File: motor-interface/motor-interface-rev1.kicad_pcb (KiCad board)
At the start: 2 copper layers, 43 parts, among them P1 CONN_02X12, P10 CONN_01X03, P11 CONN_01X04, P12 CONN_01X03, P13 CONN_01X03, P2 CONN_02X10, P3 CONN_01X03, P4 CONN_02X10, P5 CONN_01X04, P6 CONN_01X04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

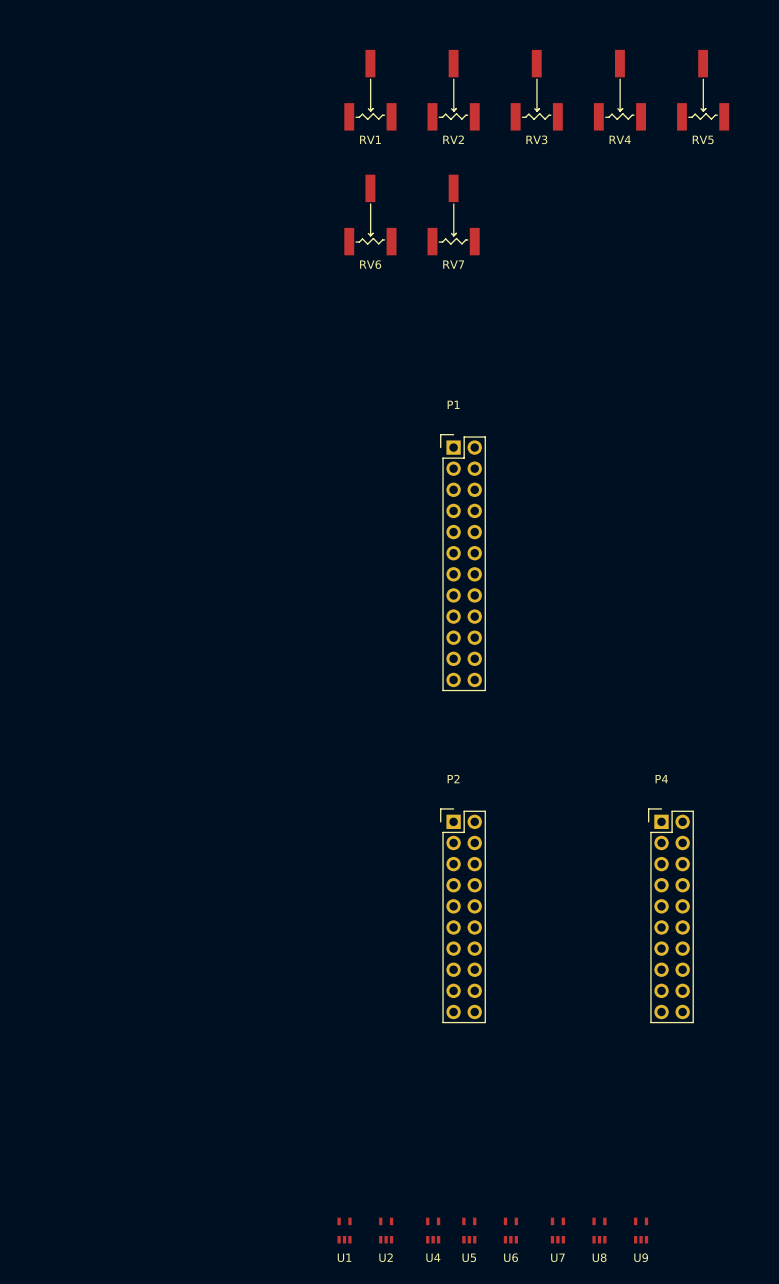
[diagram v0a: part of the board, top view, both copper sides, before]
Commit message: Created board outline
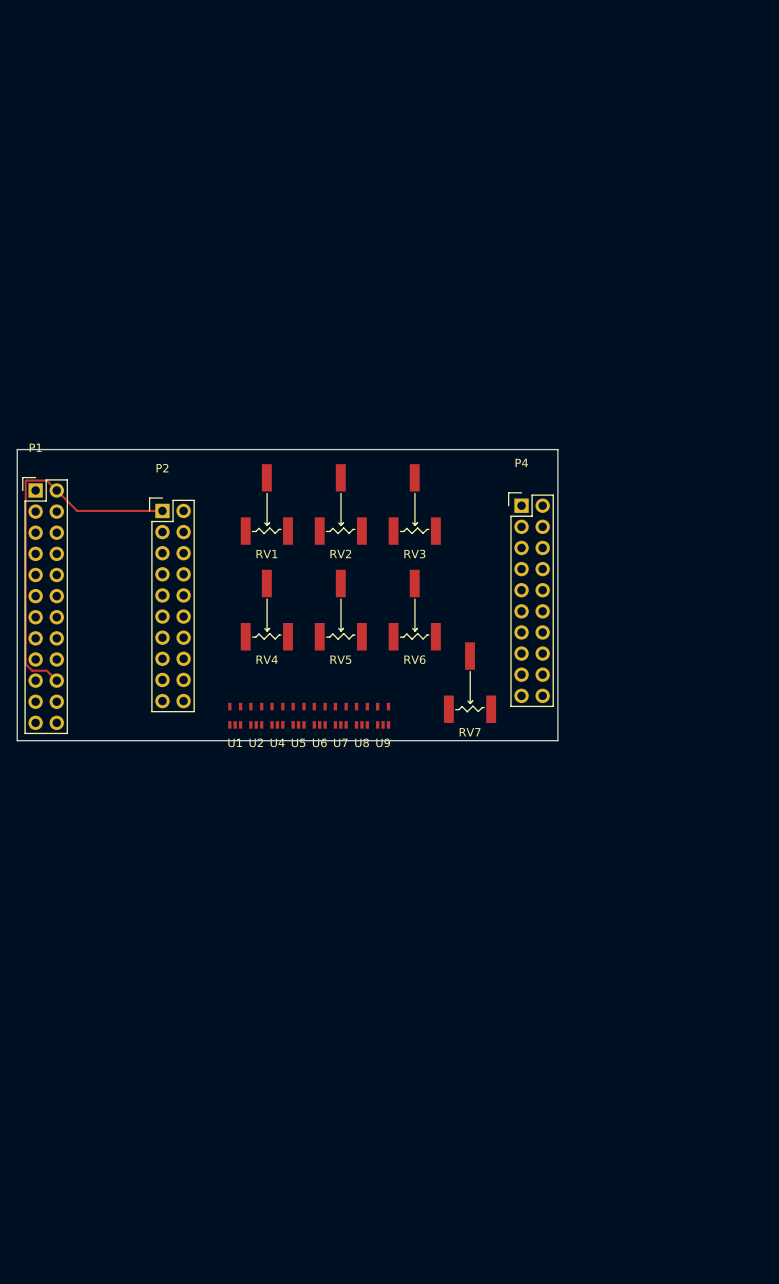
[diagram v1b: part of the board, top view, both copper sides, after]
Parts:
- moved RV5 76.2 mm to (88.9, 114.3)
- moved RV4 75.6 mm to (80.0, 114.3)
- moved U9 69.2 mm to (94.0, 127.0)
- moved U8 68.2 mm to (91.4, 127.0)
- moved U7 67.2 mm to (88.9, 127.0)
- moved U6 66.0 mm to (86.4, 127.0)
- moved U5 65.2 mm to (83.8, 127.0)
- moved U4 64.7 mm to (81.3, 127.0)
- moved U2 63.8 mm to (78.7, 127.0)
- moved U1 63.3 mm to (76.2, 127.0)
- moved RV7 56.3 mm to (104.4, 123.0)
- moved RV3 51.9 mm to (97.8, 101.6)
- moved RV2 51.6 mm to (88.9, 101.6)
- moved RV1 51.3 mm to (80.0, 101.6)
- moved P2 51.2 mm to (67.5, 102.4)
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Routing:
- net +3V3: track 0.00 -> 44.5 mm
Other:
- board outline added: 65 x 35 mm
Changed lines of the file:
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@@
   (general
     (links 117)
-    (no_connects 81)
-    (area 0 0 0 0)
+    (no_connects 116)
+    (area 84.479762 18.695 265.108334 193.175)
     (thickness 1.6)
-    (drawings 0)
-    (tracks 0)
+    (drawings 4)
+    (tracks 10)
     (zones 0)
     (modules 43)
@@
     (pad_to_mask_clearance 0.2)
     (aux_axis_origin 0 0)
-    (visible_elements FFFFFF7F)
+    (visible_elements 7FFFFFFF)
     (pcbplotparams
       (layerselection 0x00030_80000001)
@@
   )
   (module Pin_Headers:Pin_Header_Straight_2x12 (layer F.Cu)
-    (at 102.46 94.76)
+    (at 52.21 99.92)
     (descr "Through hole pin header")
     (tags "pin header")
@@
   )
   (module Pin_Headers:Pin_Header_Straight_2x10 (layer F.Cu)
-    (at 102.46 139.76)
+    (at 67.46 102.38)
     (descr "Through hole pin header")
     (tags "pin header")
@@
   )
   (module Pin_Headers:Pin_Header_Straight_2x10 (layer F.Cu)
-    (at 127.46 139.76)
+    (at 110.63 101.75)
     (descr "Through hole pin header")
     (tags "pin header")
@@
   )
   (module p16261:3361P (layer F.Cu)
-    (at 92.46 51.8)
+    (at 80.01 101.6)
     (tags POT,POTENTIOMETER)
     (fp_text reference RV1 (at 0 6) (layer F.SilkS)
@@
   )
   (module p16261:3361P (layer F.Cu)
-    (at 102.46 51.8)
+    (at 88.9 101.6)
     (tags POT,POTENTIOMETER)
     (fp_text reference RV2 (at 0 6) (layer F.SilkS)
@@
   )
   (module p16261:3361P (layer F.Cu)
-    (at 112.46 51.8)
+    (at 97.79 101.6)
     (tags POT,POTENTIOMETER)
     (fp_text reference RV3 (at 0 6) (layer F.SilkS)
@@
   )
   (module p16261:3361P (layer F.Cu)
-    (at 122.46 51.8)
+    (at 80.01 114.3)
     (tags POT,POTENTIOMETER)
     (fp_text reference RV4 (at 0 6) (layer F.SilkS)
@@
   )
   (module p16261:3361P (layer F.Cu)
-    (at 132.46 51.8)
+    (at 88.9 114.3)
     (tags POT,POTENTIOMETER)
     (fp_text reference RV5 (at 0 6) (layer F.SilkS)
@@
   )
   (module p16261:3361P (layer F.Cu)
-    (at 92.46 66.8)
+    (at 97.79 114.3)
     (tags POT,POTENTIOMETER)
     (fp_text reference RV6 (at 0 6) (layer F.SilkS)
@@
   )
   (module p16261:3361P (layer F.Cu)
-    (at 102.46 66.8)
+    (at 104.43464 123.02236)
     (tags POT,POTENTIOMETER)
     (fp_text reference RV7 (at 0 6) (layer F.SilkS)
@@
   )
   (module p16261:SN74LV1T34 (layer F.Cu)
-    (at 89.35 188.9)
+    (at 76.2 127)
     (tags "LEVEL SHIFTER")
     (fp_text reference U1 (at 0 3.3) (layer F.SilkS)
@@
   )
   (module p16261:SN74LV1T34 (layer F.Cu)
-    (at 94.35 188.9)
+    (at 78.74 127)
     (tags "LEVEL SHIFTER")
     (fp_text reference U2 (at 0 3.3) (layer F.SilkS)
@@
   )
   (module p16261:SN74LV1T34 (layer F.Cu)
-    (at 100 188.9)
+    (at 81.28 127)
     (tags "LEVEL SHIFTER")
     (fp_text reference U4 (at 0 3.3) (layer F.SilkS)
@@
   )
   (module p16261:SN74LV1T34 (layer F.Cu)
-    (at 104.35 188.9)
+    (at 83.82 127)
     (tags "LEVEL SHIFTER")
     (fp_text reference U5 (at 0 3.3) (layer F.SilkS)
@@
   )
   (module p16261:SN74LV1T34 (layer F.Cu)
-    (at 109.35 188.9)
+    (at 86.36 127)
     (tags "LEVEL SHIFTER")
     (fp_text reference U6 (at 0 3.3) (layer F.SilkS)
@@
   )
   (module p16261:SN74LV1T34 (layer F.Cu)
-    (at 115 188.9)
+    (at 88.9 127)
     (tags "LEVEL SHIFTER")
     (fp_text reference U7 (at 0 3.3) (layer F.SilkS)
@@
   )
   (module p16261:SN74LV1T34 (layer F.Cu)
-    (at 120 188.9)
+    (at 91.44 127)
     (tags "LEVEL SHIFTER")
     (fp_text reference U8 (at 0 3.3) (layer F.SilkS)
@@
   )
   (module p16261:SN74LV1T34 (layer F.Cu)
-    (at 125 188.9)
+    (at 93.98 127)
     (tags "LEVEL SHIFTER")
     (fp_text reference U9 (at 0 3.3) (layer F.SilkS)
@@
       (net 3 +3V3) (solder_mask_margin 0.05) (solder_paste_margin -0.05))
   )
+  (gr_line (start 115 130) (end 50 130) (layer Edge.Cuts) (width 0.15))
+  (gr_line (start 115 95) (end 115 130) (layer Edge.Cuts) (width 0.15))
+  (gr_line (start 50 95) (end 115 95) (layer Edge.Cuts) (width 0.15))
+  (gr_line (start 50 95) (end 50 130) (layer Edge.Cuts) (width 0.15))
+  (segment (start 54.75 99.92) (end 53.561399 98.731399) (width 0.25) (layer F.Cu) (net 3))
+  (segment (start 53.561399 98.731399) (end 51.086399 98.731399) (width 0.25) (layer F.Cu) (net 3))
+  (segment (start 51.086399 98.731399) (end 51.021399 98.796399) (width 0.25) (layer F.Cu) (net 3))
+  (segment (start 51.021399 98.796399) (end 51.021399 120.810529) (width 0.25) (layer F.Cu) (net 3))
+  (segment (start 51.021399 120.810529) (end 51.802269 121.591399) (width 0.25) (layer F.Cu) (net 3))
+  (segment (start 51.802269 121.591399) (end 53.561399 121.591399) (width 0.25) (layer F.Cu) (net 3))
+  (segment (start 53.561399 121.591399) (end 53.886401 121.916401) (width 0.25) (layer F.Cu) (net 3))
+  (segment (start 53.886401 121.916401) (end 54.75 122.78) (width 0.25) (layer F.Cu) (net 3))
+  (segment (start 54.75 99.92) (end 57.21 102.38) (width 0.25) (layer F.Cu) (net 3))
+  (segment (start 57.21 102.38) (end 67.46 102.38) (width 0.25) (layer F.Cu) (net 3))
 )

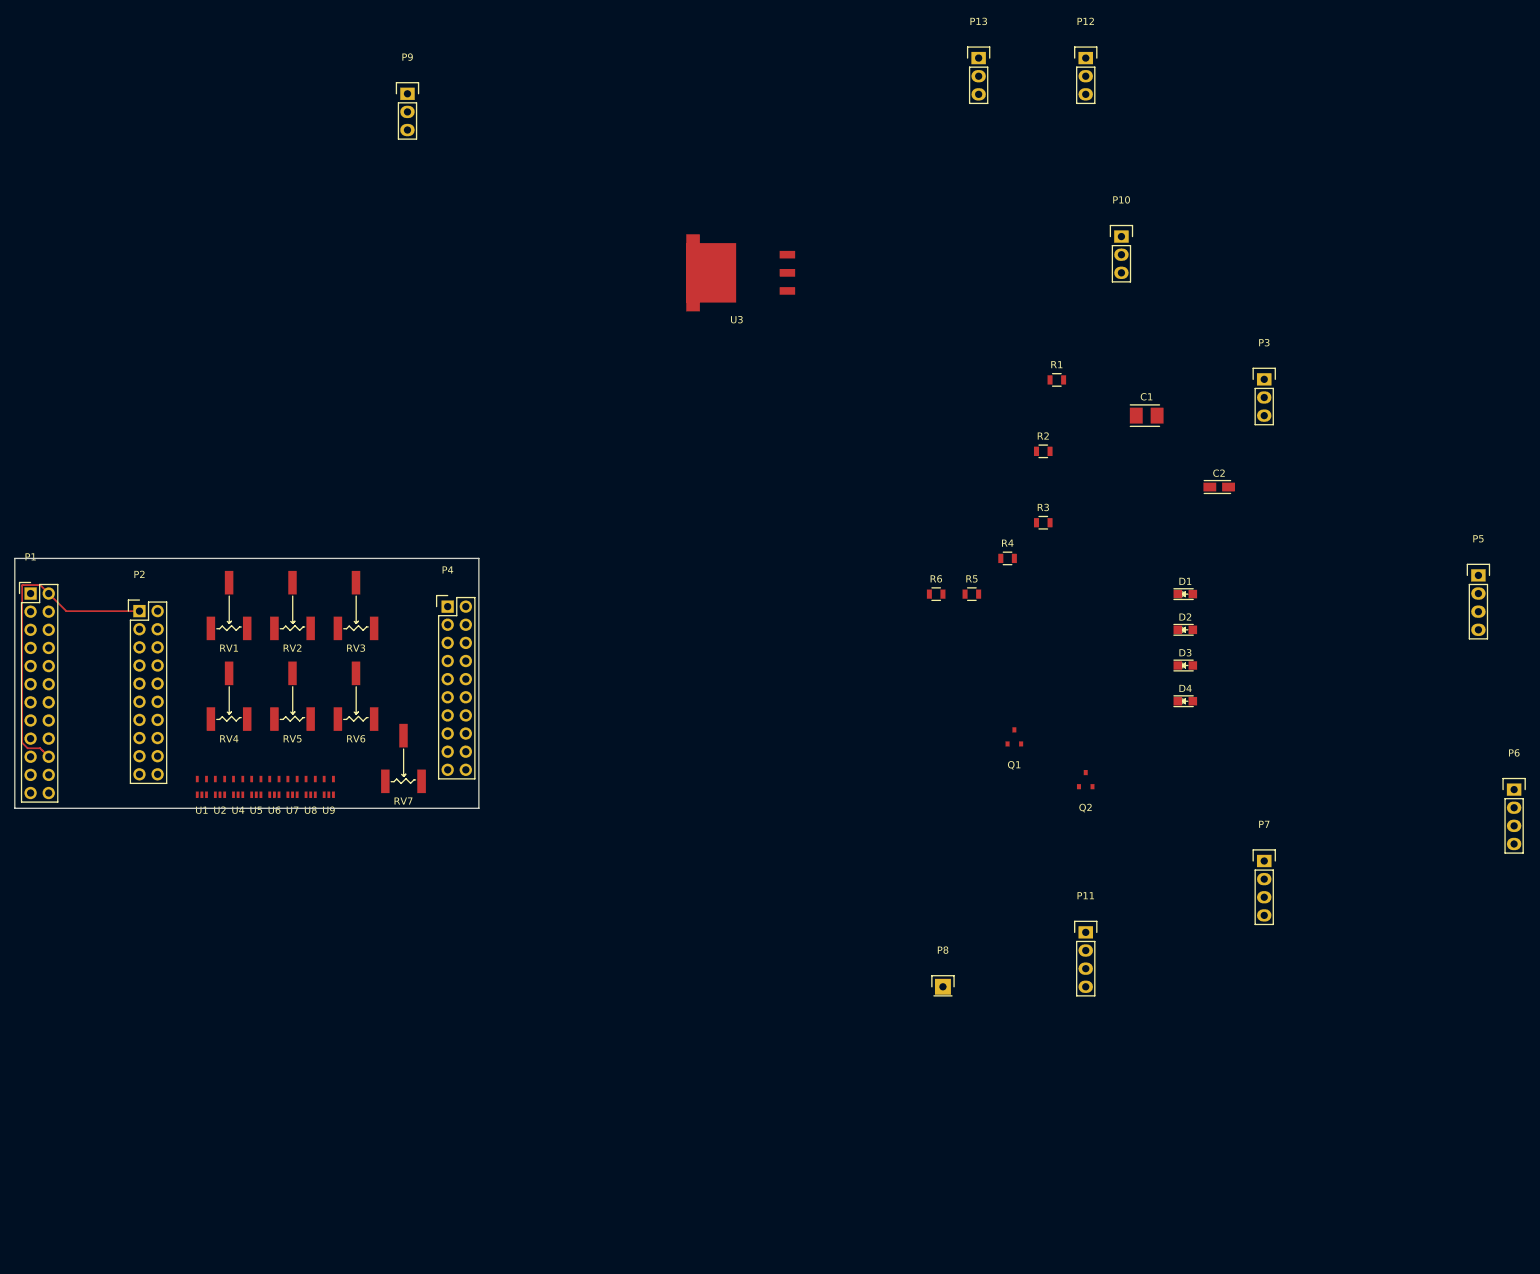
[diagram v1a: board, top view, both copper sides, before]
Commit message: Added keepouts, progress on layout
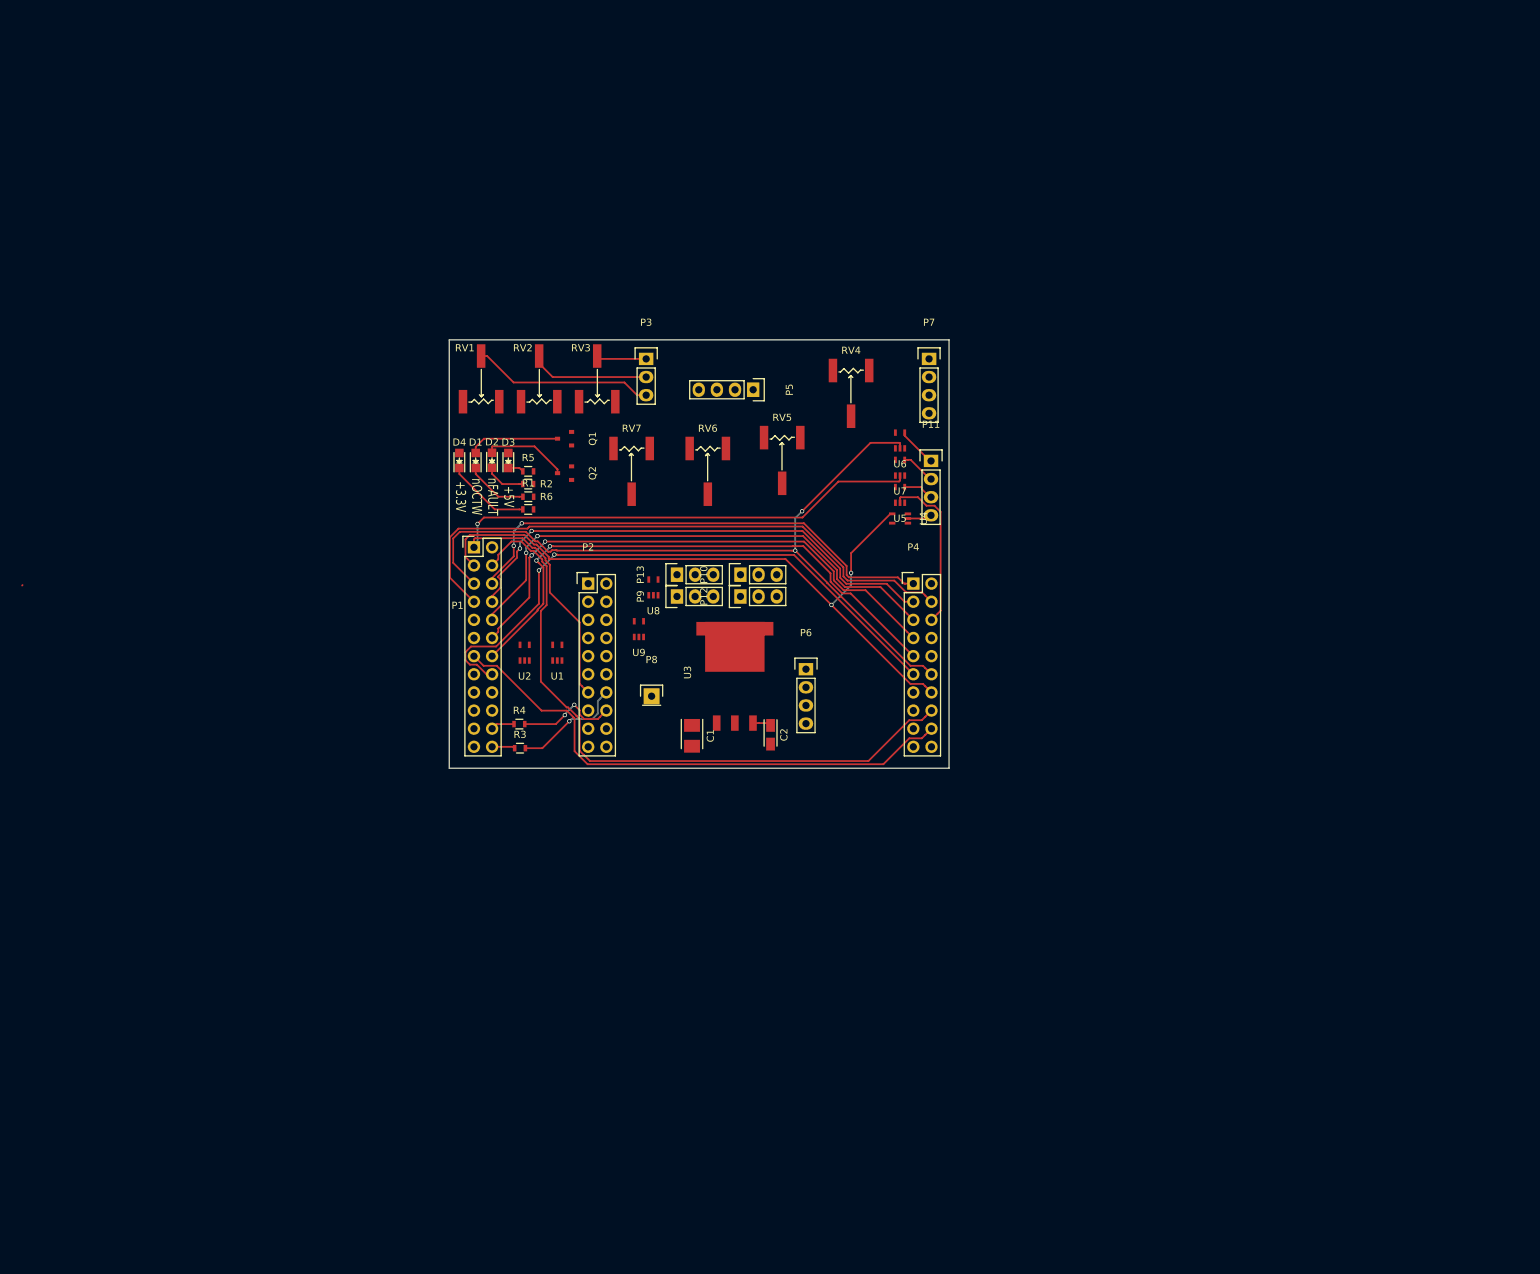
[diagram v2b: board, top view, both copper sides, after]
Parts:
- R1, R2, R3, R4, R5, R6: footprint Resistors_SMD:R_0805 -> Resistors_SMD:R_0603
- moved D4 107.1 mm to (112.3, 81.3), turned to 90 degrees
- moved P5 104.9 mm to (153.4, 71.4), turned to 270 degrees
- moved D1 101.1 mm to (114.6, 81.3), turned to 90 degrees
- moved P6 100.6 mm to (160.8, 110.5)
- moved U6 100.2 mm to (174.0, 78.5)
- moved U4 100.0 mm to (174.0, 89.4), turned to 90 degrees
- moved D2 100.0 mm to (116.8, 81.2), turned to 90 degrees
- moved D3 99.1 mm to (119.1, 81.3), turned to 90 degrees
- moved U5 99.0 mm to (174.0, 86.1)
- moved RV4 96.9 mm to (167.1, 71.9), turned to 180 degrees
- moved U7 96.1 mm to (174.0, 82.3)
- moved P12 89.6 mm to (151.6, 100.3), turned to 90 degrees
- moved P3 86.6 mm to (138.4, 67.1)
- moved Q2 84.7 mm to (127.0, 83.1), turned to 90 degrees
- moved P7 84.6 mm to (178.1, 67.1)
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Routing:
- net Net-(P1-Pad5): track 0.00 -> 107.7 mm, vias 0 -> 2
- net Net-(P1-Pad1): track 0.00 -> 99.5 mm, vias 0 -> 1
- net Net-(P1-Pad3): track 0.00 -> 95.4 mm, vias 0 -> 2
- net Net-(P1-Pad4): track 0.00 -> 92.4 mm
- net Net-(P1-Pad16): track 0.00 -> 83.8 mm, vias 0 -> 2
- net Net-(P1-Pad7): track 0.00 -> 83.6 mm
- net Net-(P1-Pad14): track 0.00 -> 77.5 mm, vias 0 -> 2
- net Net-(P1-Pad13): track 0.00 -> 75.1 mm
- net Net-(P1-Pad12): track 0.00 -> 74.5 mm, vias 0 -> 2
- net Net-(P1-Pad10): track 0.00 -> 72.6 mm, vias 0 -> 2
- net Net-(P1-Pad8): track 0.00 -> 70.8 mm, vias 0 -> 2
- net Net-(P1-Pad6): track 0.00 -> 69.3 mm, vias 0 -> 2
- net +3V3: track 44.5 -> 2.76 mm
- net Net-(P2-Pad14): track 0.00 -> 41.0 mm, vias 0 -> 2
- net Net-(P2-Pad16): track 0.00 -> 31.1 mm, vias 0 -> 2
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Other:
- board size 65 x 35 mm -> 70 x 60 mm
- board text added: "+5V nFAULT nOCTW +3.3V"
